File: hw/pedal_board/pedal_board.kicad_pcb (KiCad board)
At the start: 2 copper layers, 94 x 47 mm, 7 parts, among them J1 Conn_01x04, J2 Conn_01x02

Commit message: Add files of pedal_board v2
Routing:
- net GND: track 7.62 -> 14.6 mm
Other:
- net class Default: trace_width 0.25 -> 0.5
- board text added: "+Vin"
- board text added: "Arduino RF Nano"
- board text added: "GND"
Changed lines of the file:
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@@
   (general
     (thickness 1.6)
-    (drawings 8)
-    (tracks 29)
+    (drawings 26)
+    (tracks 30)
     (zones 0)
     (modules 7)
@@
   )
   (setup
-    (last_trace_width 0.25)
+    (last_trace_width 0.5)
     (trace_clearance 0.2)
     (zone_clearance 0.508)
@@
   (net_class Default "This is the default net class."
     (clearance 0.2)
-    (trace_width 0.25)
+    (trace_width 0.5)
     (via_dia 0.6)
     (via_drill 0.4)
@@
     (pad 1 thru_hole circle (at 0 0) (size 6.4 6.4) (drill 3.2) (layers *.Cu *.Mask))
   )
+  (gr_line (start 204.47 70.485) (end 204.47 74.295) (layer F.SilkS) (width 0.15))
+  (gr_line (start 209.55 78.105) (end 209.55 80.01) (layer F.SilkS) (width 0.15))
+  (gr_line (start 206.375 78.105) (end 209.55 78.105) (layer F.SilkS) (width 0.15))
+  (gr_line (start 206.375 76.835) (end 206.375 78.105) (layer F.SilkS) (width 0.15))
+  (gr_line (start 209.55 76.835) (end 206.375 76.835) (layer F.SilkS) (width 0.15))
+  (gr_line (start 209.55 75.565) (end 209.55 76.835) (layer F.SilkS) (width 0.15))
+  (gr_line (start 206.375 75.565) (end 209.55 75.565) (layer F.SilkS) (width 0.15))
+  (gr_line (start 206.375 74.295) (end 206.375 75.565) (layer F.SilkS) (width 0.15))
+  (gr_line (start 209.55 74.295) (end 206.375 74.295) (layer F.SilkS) (width 0.15))
+  (gr_line (start 209.55 73.025) (end 209.55 74.295) (layer F.SilkS) (width 0.15))
+  (gr_line (start 206.375 73.025) (end 209.55 73.025) (layer F.SilkS) (width 0.15))
+  (gr_line (start 206.375 71.755) (end 206.375 73.025) (layer F.SilkS) (width 0.15))
+  (gr_line (start 209.55 71.755) (end 206.375 71.755) (layer F.SilkS) (width 0.15))
+  (gr_line (start 209.55 70.485) (end 209.55 71.755) (layer F.SilkS) (width 0.15))
+  (gr_line (start 203.2 70.485) (end 209.55 70.485) (layer F.SilkS) (width 0.15))
+  (gr_text GND (at 210.185 92.71) (layer F.SilkS)
+    (effects (font (size 1 1) (thickness 0.15)))
+  )
+  (gr_text +Vin (at 210.185 90.17) (layer F.SilkS)
+    (effects (font (size 1 1) (thickness 0.15)))
+  )
+  (gr_text "Arduino RF Nano" (at 189.23 74.295) (layer F.SilkS)
+    (effects (font (size 1 1) (thickness 0.15)))
+  )
   (gr_line (start 191.5 88) (end 191.5 105.5) (layer Edge.Cuts) (width 0.1))
   (gr_line (start 184.5 88) (end 191.5 88) (layer Edge.Cuts) (width 0.1))
@@
   (gr_line (start 191.5 105.5) (end 235 105.5) (layer Edge.Cuts) (width 0.1))
   (gr_line (start 141 105.5) (end 184.5 105.5) (layer Edge.Cuts) (width 0.1))
+  (segment (start 173.99 91.44) (end 167.005 91.44) (width 1) (layer F.Cu) (net 1))
   (segment (start 204.47 90.17) (end 204.47 82.55) (width 0.25) (layer F.Cu) (net 1))
   (segment (start 207.01 90.17) (end 207.01 82.55) (width 0.25) (layer F.Cu) (net 2))

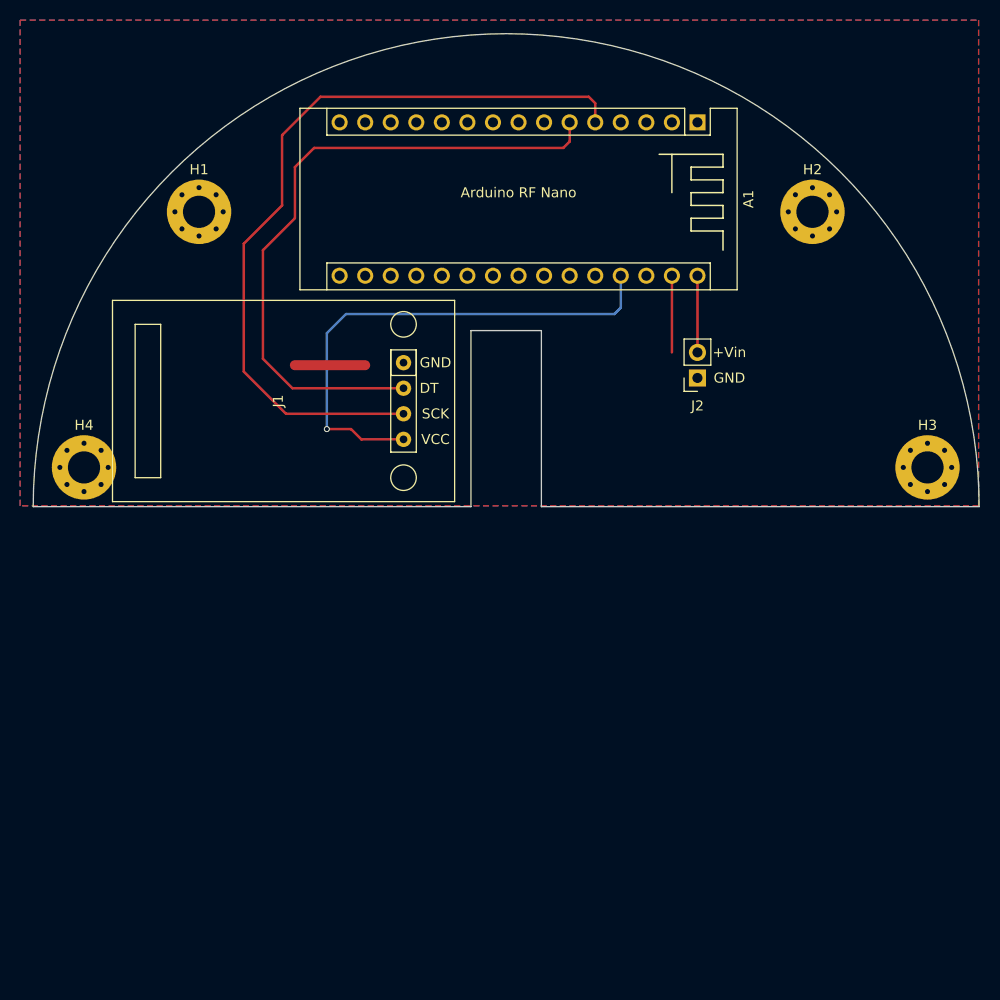
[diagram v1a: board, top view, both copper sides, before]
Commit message: Add Panelization test
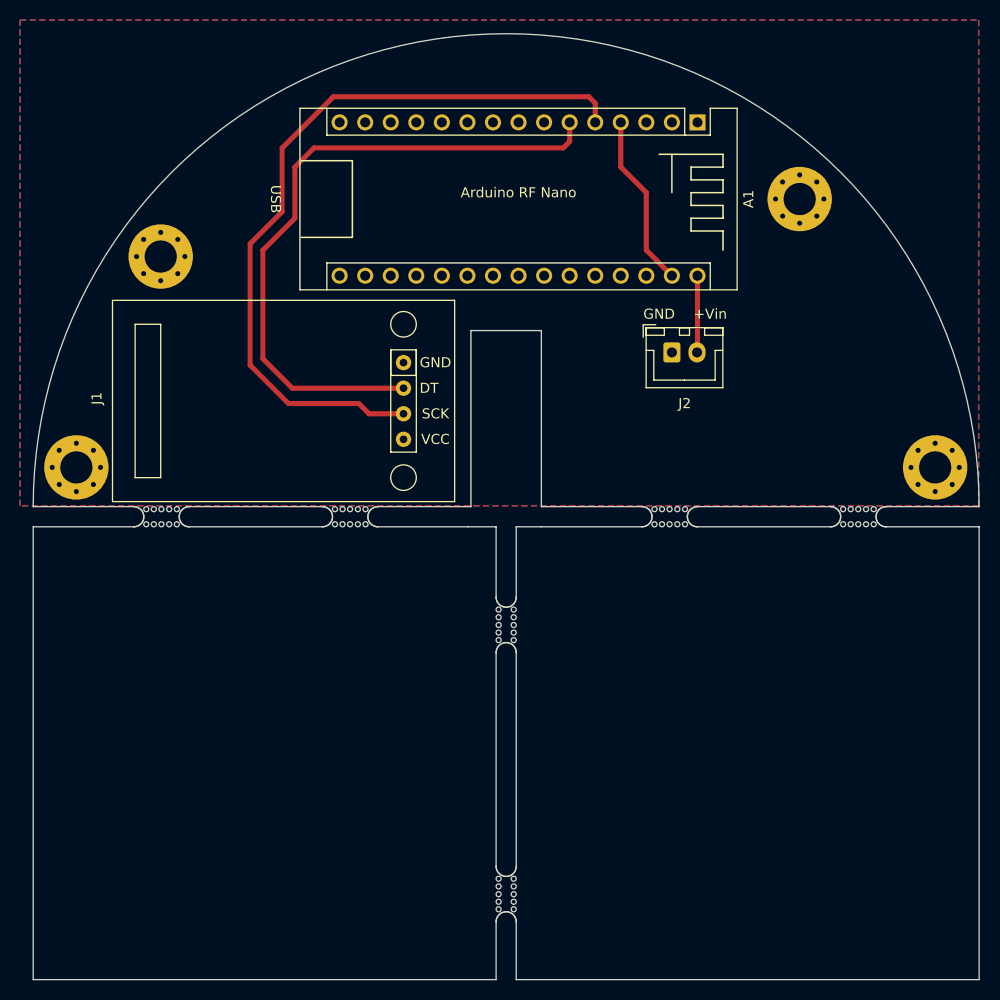
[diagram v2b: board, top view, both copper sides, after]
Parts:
- added G***: LOGO, lconos:logo_fiuner, B.Cu at (163.2, 94.0)
- added REF**: KiCad-Logo2_6mm_SilkScreen, Symbol:KiCad-Logo2_6mm_SilkScreen, B.Cu at (218.4, 94.0)
- added mouse-bite-3mm-slot: VAL**, Panelization:mouse-bite-3mm-slot, F.Cu at (188.0, 144.0)
- added mouse-bite-3mm-slot: VAL**, Panelization:mouse-bite-3mm-slot, F.Cu at (188.0, 117.2)
- added mouse-bite-3mm-slot: VAL**, Panelization:mouse-bite-3mm-slot, F.Cu at (204.2, 106.5)
- added mouse-bite-3mm-slot: VAL**, Panelization:mouse-bite-3mm-slot, F.Cu at (223.0, 106.5)
- added mouse-bite-3mm-slot: VAL**, Panelization:mouse-bite-3mm-slot, F.Cu at (172.5, 106.5)
- added mouse-bite-3mm-slot: VAL**, Panelization:mouse-bite-3mm-slot, F.Cu at (153.8, 106.5)
- J2: footprint Connector_PinSocket_2.54mm:PinSocket_1x02_P2.54mm_Vertical -> Connector_JST:JST_XH_B2B-XH-A_1x02_P2.50mm_Vertical
- moved H1 5.85 mm to (153.7, 80.6)
- moved J2 3.59 mm to (204.5, 90.2), turned to 0 degrees
- moved H2 1.80 mm to (217.2, 74.9)
- moved H3 0.76 mm to (230.6, 101.6)
- moved H4 0.76 mm to (145.3, 101.6)
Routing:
- net +5V: track 51.0 -> 0.00 mm, vias 1 -> 0
- net GND: track 14.6 -> 17.3 mm
- net /SCK: track 77.5 -> 75.5 mm
- added copper zone on B.Cu, net +5V
- removed copper zone on B.Cu, net (none)
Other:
- board size 94 x 47 mm -> 94 x 94 mm
- board text added: "Pedal_Board V2"
- board text added: "USB"

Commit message: Add 3d models, send to review pcb
review the 3d model of hx711
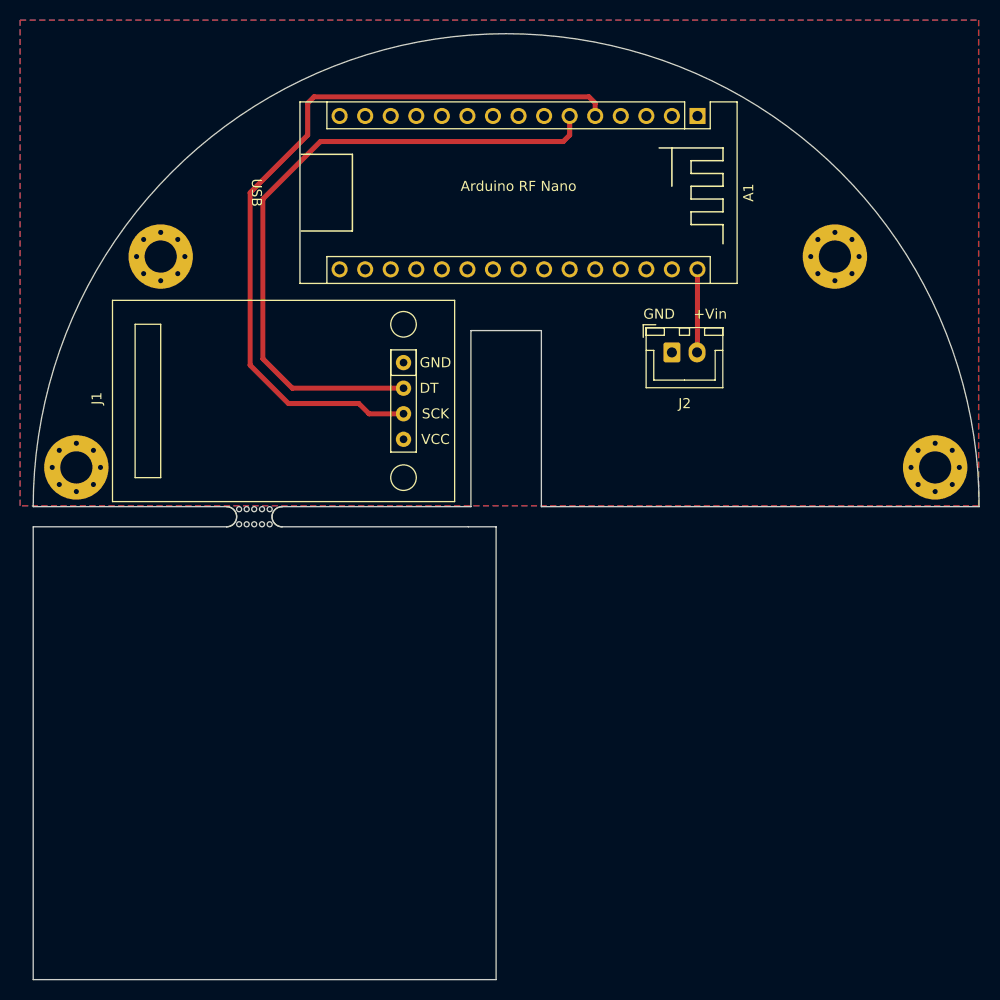
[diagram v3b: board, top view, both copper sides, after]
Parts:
- removed the mouse-bite-3mm-slot at (188.0, 144.0)
- removed the mouse-bite-3mm-slot at (188.0, 117.2)
- removed the mouse-bite-3mm-slot at (204.2, 106.5)
- removed the mouse-bite-3mm-slot at (223.0, 106.5)
- removed the mouse-bite-3mm-slot at (172.5, 106.5)
- removed the mouse-bite-3mm-slot at (153.8, 106.5)
- added mouse-bite-3mm-slot: VAL**, Panelization:mouse-bite-3mm-slot, F.Cu at (163.0, 106.5)
- moved H2 6.70 mm to (220.7, 80.6)
- moved A1 0.64 mm to (207.0, 66.7)
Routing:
- net GND: track 17.3 -> 0.00 mm
- net /Vin: track 7.62 -> 8.27 mm
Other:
- outline, holes or cut-outs redrawn
